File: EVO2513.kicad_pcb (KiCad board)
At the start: 8 copper layers, 110 x 69 mm, 271 parts, among them J1 1053101204, J2 1053101114, J3 10144517-043802LF, J4 1053102204, J5 1053091102, J6 1053091102, M1 78614150960, M2 78614150960, M3 78614150960, M4 78614150960, M5 78614150960, M6 78614150960, Q1 DMT6007LFGQ-7, Q10 DMT4011LFG, Q11 DMT4011LFG, Q12 DMP3007SCG-13, Q13 DMP3007SCG-13, Q14 DMP3007SCG-13, Q15 DMP3007SCG-13, Q16 IAUCN04S7L019, Q17 IAUCN04S7L028, Q18 CSD17304Q3, Q19 IAUCN04S7L019, Q20 BSS138, Q21 BSS138, Q22 BSS138, Q23 BSS138, Q24 BSS138, Q3 DMT6007LFGQ-7, Q4 DMP3007SCG-13, Q5 DMP3007SCG-13, Q6 DMT4011LFG, Q7 DMT4011LFG, Q8 DMT4011LFG, Q9 DMT4011LFG, U1 LTC1960, U10 TLV9002IDSG, U11 PCAL9714, U2 LTC4365, U5 LM51772RHAR, U6 TPS22811, U7 TPS22811, U8 TLV9002IDSG, U9 TPS22811

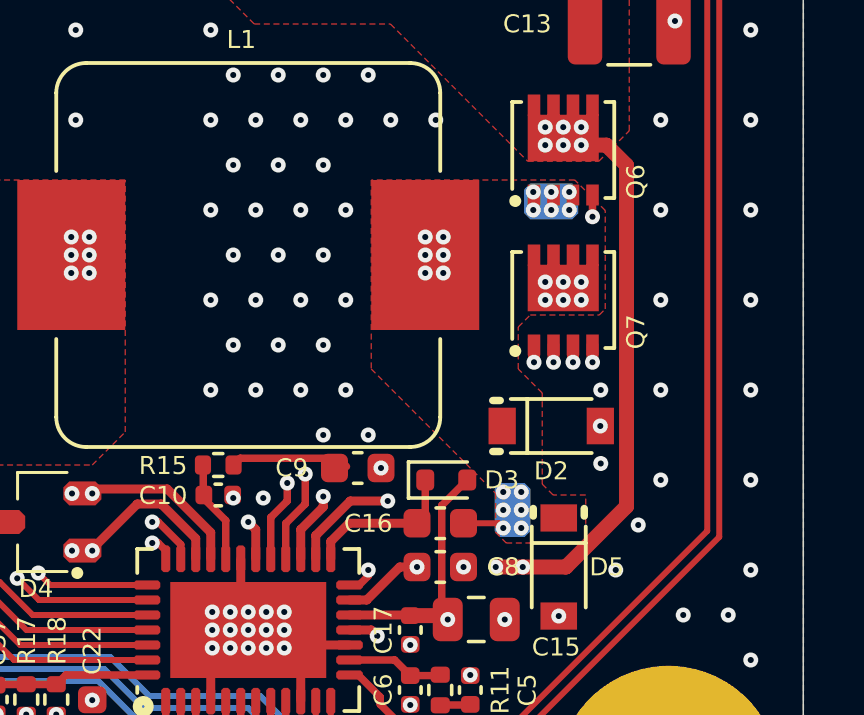
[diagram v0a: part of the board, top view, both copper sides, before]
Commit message: Trim the charger switch-node pours to the current path
The SW (Net-(D2-C)) pours covered x 189-197, y 115-127 on F.Cu, In2 and
In4, but only the Q6/Q7/L1 strip carries inductor current.

- In2 and In4: cut back to the strip (y 115.0-119.7).
- F.Cu: keep the strip plus a 1.3 mm neck to D2's cathode, D5 and the
  pin-19 via; drop the wedge between L1 and the old diagonal edge.
- Remove five stitching vias in the south tail that would now only
  reach F.Cu.

SW copper 186 -> 123 mm2; the freed area fills with GND.
DRC unchanged: 0 unconnected, 0 parity.

Co-Authored-By: Claude Opus 5.5 <noreply@anthropic.com>
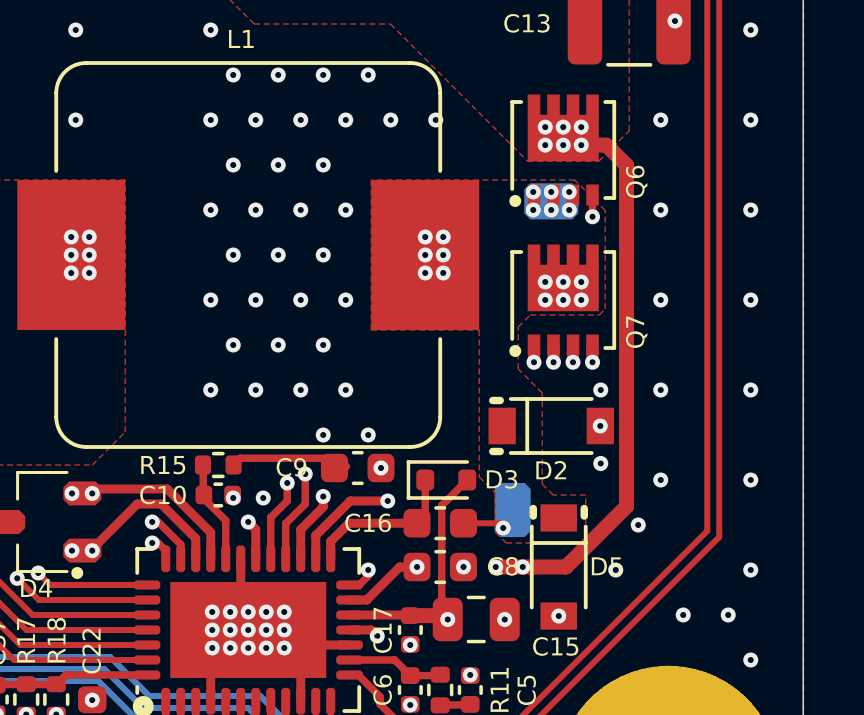
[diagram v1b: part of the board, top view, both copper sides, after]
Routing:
- net Net-(D2-C): vias 25 -> 20
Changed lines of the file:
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@@
 	)
 	(via
-		(at 193.5011 126.0036)
-		(size 0.5)
-		(drill 0.2)
-		(layers "F.Cu" "B.Cu")
-		(teardrops
-			(best_length_ratio 0.4)
-			(max_length 1)
-			(best_width_ratio 0.9)
-			(max_width 2)
-			(curved_edges no)
-			(filter_ratio 0.8)
-			(enabled yes)
-			(allow_two_segments yes)
-			(prefer_zone_connections yes)
-		)
-		(net "Net-(D2-C)")
-	)
-	(via
-		(at 193.5011 125.4036)
-		(size 0.5)
-		(drill 0.2)
-		(layers "F.Cu" "B.Cu")
-		(teardrops
-			(best_length_ratio 0.4)
-			(max_length 1)
-			(best_width_ratio 0.9)
-			(max_width 2)
-			(curved_edges no)
-			(filter_ratio 0.8)
-			(enabled yes)
-			(allow_two_segments yes)
-			(prefer_zone_connections yes)
-		)
-		(net "Net-(D2-C)")
-	)
-	(via
 		(at 195.1011 116.0036)
 		(size 0.5)
@@
 	)
 	(via
-		(at 194.1011 126.0036)
-		(size 0.5)
-		(drill 0.2)
-		(layers "F.Cu" "B.Cu")
-		(teardrops
-			(best_length_ratio 0.4)
-			(max_length 1)
-			(best_width_ratio 0.9)
-			(max_width 2)
-			(curved_edges no)
-			(filter_ratio 0.8)
-			(enabled yes)
-			(allow_two_segments yes)
-			(prefer_zone_connections yes)
-		)
-		(net "Net-(D2-C)")
-	)
-	(via
-		(at 194.1011 125.4036)
-		(size 0.5)
-		(drill 0.2)
-		(layers "F.Cu" "B.Cu")
-		(teardrops
-			(best_length_ratio 0.4)
-			(max_length 1)
-			(best_width_ratio 0.9)
-			(max_width 2)
-			(curved_edges no)
-			(filter_ratio 0.8)
-			(enabled yes)
-			(allow_two_segments yes)
-			(prefer_zone_connections yes)
-		)
-		(net "Net-(D2-C)")
-	)
-	(via
 		(at 190.9011 116.9036)
 		(size 0.5)
@@
 	)
 	(via
-		(at 194.1011 126.6036)
-		(size 0.5)
-		(drill 0.2)
-		(layers "F.Cu" "B.Cu")
-		(teardrops
-			(best_length_ratio 0.4)
-			(max_length 1)
-			(best_width_ratio 0.9)
-			(max_width 2)
-			(curved_edges no)
-			(filter_ratio 0.8)
-			(enabled yes)
-			(allow_two_segments yes)
-			(prefer_zone_connections yes)
-		)
-		(net "Net-(D2-C)")
-	)
-	(via
 		(at 196.1011 118.4036)
 		(size 0.5)
@@
 		(polygon
 			(pts
-				(xy 189.1011 115.0036) (xy 189.1011 121.3036) (xy 193.2456 125.4481) (xy 193.2456 126.7481) (xy 193.6011 127.1036)
-				(xy 196.2511 127.1036) (xy 196.2511 125.5036) (xy 195.1636 125.5036) (xy 194.8011 125.1411) (xy 194.8011 122.1036)
-				(xy 194.0011 121.3036) (xy 194.0011 119.9036) (xy 194.4011 119.5036) (xy 196.7011 119.5036) (xy 196.9011 119.3036)
-				(xy 196.9011 116.01861) (xy 195.88609 115.0036)
+				(xy 189.1011 115.0036) (xy 189.1011 120.0036) (xy 192.7011 120.0036) (xy 192.7011 124.9036) (xy 193.2456 125.4481) (xy 193.2456 126.7481) (xy 193.6011 127.1036) (xy 196.2511 127.1036) (xy 196.2511 125.5036) (xy 195.1636 125.5036) (xy 194.8011 125.1411) (xy 194.8011 122.1036) (xy 194.0011 121.3036) (xy 194.0011 119.9036) (xy 194.4011 119.5036) (xy 196.7011 119.5036) (xy 196.9011 119.3036) (xy 196.9011 116.01861) (xy 195.88609 115.0036)
 			)
 		)
@@
 		(polygon
 			(pts
-				(xy 189.1011 115.0036) (xy 189.1011 121.279336) (xy 193.1011 125.279336) (xy 193.1011 126.7036)
-				(xy 193.5011 127.1036) (xy 194.2011 127.1036) (xy 194.6011 126.7036) (xy 194.6011 124.3036) (xy 194.6011 119.9036)
-				(xy 194.8011 119.7036) (xy 197.0011 119.7036) (xy 197.2011 119.5036) (xy 197.2011 116.31861) (xy 195.88609 115.0036)
+				(xy 189.1011 115.0036) (xy 189.1011 119.7036) (xy 197.0011 119.7036) (xy 197.2011 119.5036) (xy 197.2011 116.31861) (xy 195.88609 115.0036)
 			)
 		)
@@
 		(polygon
 			(pts
-				(xy 189.1011 115.0036) (xy 189.1011 121.7036) (xy 193.0011 125.6036) (xy 193.0011 126.6036) (xy 193.5011 127.1036)
-				(xy 194.2011 127.1036) (xy 194.6011 126.7036) (xy 194.6011 121.9036) (xy 194.6011 120.5036) (xy 195.4011 119.7036)
-				(xy 197.0011 119.7036) (xy 197.2011 119.5036) (xy 197.2011 116.31861) (xy 195.88609 115.0036)
+				(xy 189.1011 115.0036) (xy 189.1011 119.7036) (xy 197.0011 119.7036) (xy 197.2011 119.5036) (xy 197.2011 116.31861) (xy 195.88609 115.0036)
 			)
 		)
